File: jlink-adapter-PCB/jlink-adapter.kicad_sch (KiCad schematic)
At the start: 13 parts, among them J1 Conn_02x10_Odd_Even, J2 Conn_02x05_Odd_Even, J3 Conn_02x05_Odd_Even, Q1 BSS123TA

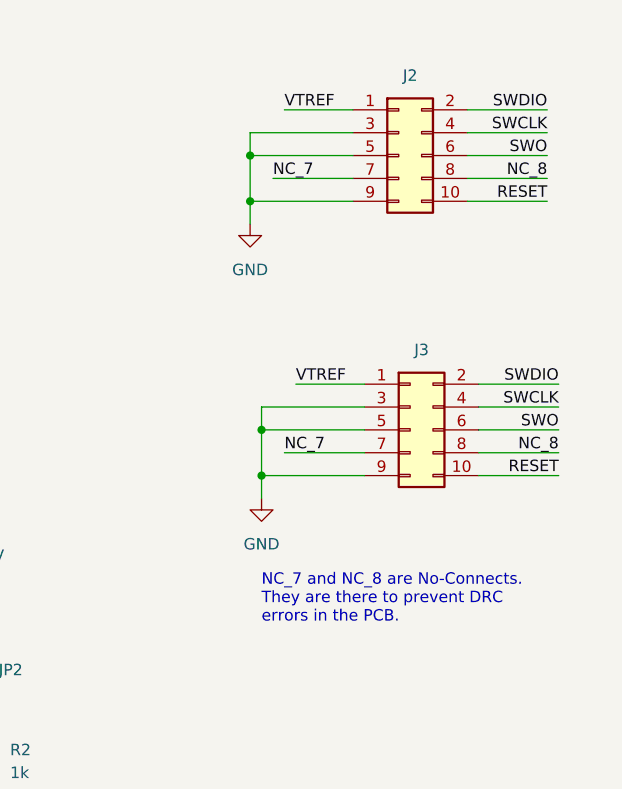
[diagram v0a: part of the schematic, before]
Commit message: Consolidate 10-pin connection on schematic
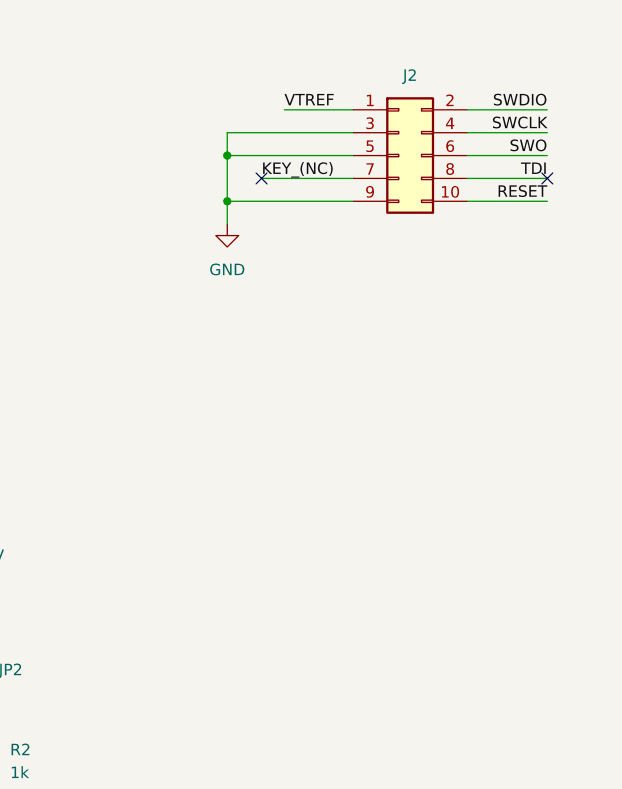
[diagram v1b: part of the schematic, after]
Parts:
- removed J3: Conn_02x05_Odd_Even, Connector_PinHeader_1.27mm:PinHeader_2x05_P1.27mm_Vertical_SMD, symbol Connector_Generic:Conn_02x05_Odd_Even
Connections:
- net NC_7 renamed KEY_(NC)
- net NC_8 renamed TDI
- no-connect marks 9 -> 11
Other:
- note removed: "NC_7 and NC_8 are No-Connects. They are there to prevent DRC errors in the PCB."
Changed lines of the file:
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@@
   (junction (at 93.98 124.46) (diameter 0) (color 0 0 0 0)
   )
-  (junction (at 147.32 67.31) (diameter 0) (color 0 0 0 0)
-  )
-  (junction (at 147.32 72.39) (diameter 0) (color 0 0 0 0)
-  )
-  (junction (at 146.05 36.83) (diameter 0) (color 0 0 0 0)
+  (junction (at 143.51 36.83) (diameter 0) (color 0 0 0 0)
   )
   (junction (at 34.29 45.72) (diameter 0) (color 0 0 0 0)
@@
   (junction (at 71.12 31.75) (diameter 0) (color 0 0 0 0)
   )
-  (junction (at 146.05 41.91) (diameter 0) (color 0 0 0 0)
+  (junction (at 143.51 41.91) (diameter 0) (color 0 0 0 0)
   )
   (junction (at 71.12 39.37) (diameter 0) (color 0 0 0 0)
@@
   (no_connect (at 66.04 49.53))
   (no_connect (at 66.04 46.99))
+  (no_connect (at 147.32 39.37))
   (no_connect (at 53.34 31.75))
   (no_connect (at 66.04 26.67))
+  (no_connect (at 179.07 39.37))
   (no_connect (at 53.34 39.37))
   (no_connect (at 53.34 46.99))
@@
     (stroke (width 0) (type default))
   )
-  (wire (pts (xy 146.05 36.83) (xy 157.48 36.83))
-    (stroke (width 0) (type default))
-  )
-  (wire (pts (xy 146.05 41.91) (xy 157.48 41.91))
+  (wire (pts (xy 143.51 36.83) (xy 157.48 36.83))
+    (stroke (width 0) (type default))
+  )
+  (wire (pts (xy 143.51 41.91) (xy 157.48 41.91))
     (stroke (width 0) (type default))
   )
@@
     (stroke (width 0) (type default))
   )
-  (wire (pts (xy 147.32 72.39) (xy 147.32 74.93))
-    (stroke (width 0) (type default))
-  )
   (wire (pts (xy 170.18 39.37) (xy 179.07 39.37))
     (stroke (width 0) (type default))
@@
     (stroke (width 0) (type default))
   )
-  (wire (pts (xy 171.45 69.85) (xy 180.34 69.85))
-    (stroke (width 0) (type default))
-  )
-  (wire (pts (xy 171.45 72.39) (xy 180.34 72.39))
-    (stroke (width 0) (type default))
-  )
   (wire (pts (xy 106.68 127) (xy 106.68 124.46))
     (stroke (width 0) (type default))
@@
     (stroke (width 0) (type default))
   )
-  (wire (pts (xy 146.05 34.29) (xy 157.48 34.29))
-    (stroke (width 0) (type default))
-  )
-  (wire (pts (xy 151.13 62.23) (xy 158.75 62.23))
-    (stroke (width 0) (type default))
-  )
-  (wire (pts (xy 146.05 41.91) (xy 146.05 44.45))
+  (wire (pts (xy 143.51 34.29) (xy 157.48 34.29))
+    (stroke (width 0) (type default))
+  )
+  (wire (pts (xy 143.51 41.91) (xy 143.51 44.45))
     (stroke (width 0) (type default))
   )
@@
     (stroke (width 0) (type default))
   )
-  (wire (pts (xy 147.32 64.77) (xy 147.32 67.31))
-    (stroke (width 0) (type default))
-  )
-  (wire (pts (xy 148.59 39.37) (xy 157.48 39.37))
-    (stroke (width 0) (type default))
-  )
   (wire (pts (xy 44.45 44.45) (xy 53.34 44.45))
     (stroke (width 0) (type default))
@@
     (stroke (width 0) (type default))
   )
-  (wire (pts (xy 146.05 34.29) (xy 146.05 36.83))
+  (wire (pts (xy 143.51 34.29) (xy 143.51 36.83))
     (stroke (width 0) (type default))
   )
@@
     (stroke (width 0) (type default))
   )
-  (wire (pts (xy 147.32 64.77) (xy 158.75 64.77))
-    (stroke (width 0) (type default))
-  )
   (wire (pts (xy 72.39 124.46) (xy 80.01 124.46))
     (stroke (width 0) (type default))
@@
     (stroke (width 0) (type default))
   )
-  (wire (pts (xy 171.45 67.31) (xy 180.34 67.31))
-    (stroke (width 0) (type default))
-  )
   (wire (pts (xy 71.12 31.75) (xy 71.12 34.29))
     (stroke (width 0) (type default))
@@
     (stroke (width 0) (type default))
   )
-  (wire (pts (xy 146.05 36.83) (xy 146.05 41.91))
+  (wire (pts (xy 143.51 36.83) (xy 143.51 41.91))
+    (stroke (width 0) (type default))
+  )
+  (wire (pts (xy 147.32 39.37) (xy 157.48 39.37))
     (stroke (width 0) (type default))
   )
@@
     (stroke (width 0) (type default))
   )
-  (wire (pts (xy 171.45 64.77) (xy 180.34 64.77))
-    (stroke (width 0) (type default))
-  )
-  (wire (pts (xy 149.86 69.85) (xy 158.75 69.85))
-    (stroke (width 0) (type default))
-  )
-  (wire (pts (xy 147.32 67.31) (xy 158.75 67.31))
-    (stroke (width 0) (type default))
-  )
   (wire (pts (xy 170.18 36.83) (xy 179.07 36.83))
     (stroke (width 0) (type default))
@@
     (stroke (width 0) (type default))
   )
-  (wire (pts (xy 171.45 62.23) (xy 180.34 62.23))
-    (stroke (width 0) (type default))
-  )
   (wire (pts (xy 71.12 39.37) (xy 66.04 39.37))
     (stroke (width 0) (type default))
@@
     (stroke (width 0) (type default))
   )
-  (wire (pts (xy 147.32 67.31) (xy 147.32 72.39))
-    (stroke (width 0) (type default))
-  )
-  (wire (pts (xy 147.32 72.39) (xy 158.75 72.39))
-    (stroke (width 0) (type default))
-  )
   (wire (pts (xy 53.34 49.53) (xy 34.29 49.53))
     (stroke (width 0) (type default))
-  )
-  (text "NC_7 and NC_8 are No-Connects.\nThey are there to prevent DRC\nerrors in the PCB."
-    (at 147.32 88.9 0)
-    (effects (font (size 1.27 1.27)) (justify left bottom))
-  )
-  (label "SWCLK" (at 180.34 64.77 180) (fields_autoplaced)
-    (effects (font (size 1.27 1.27)) (justify right bottom))
-  )
-  (label "NC_7" (at 149.86 69.85 0) (fields_autoplaced)
-    (effects (font (size 1.27 1.27)) (justify left bottom))
-  )
-  (label "NC_8" (at 180.34 69.85 180) (fields_autoplaced)
-    (effects (font (size 1.27 1.27)) (justify right bottom))
   )
   (label "SWDIO" (at 44.45 34.29 0) (fields_autoplaced)
@@
     (effects (font (size 1.27 1.27)) (justify right bottom))
   )
-  (label "NC_8" (at 179.07 39.37 180) (fields_autoplaced)
+  (label "TDI" (at 179.07 39.37 180) (fields_autoplaced)
     (effects (font (size 1.27 1.27)) (justify right bottom))
   )
@@
     (effects (font (size 1.27 1.27)) (justify right bottom))
   )
-  (label "RESET" (at 180.34 72.39 180) (fields_autoplaced)
-    (effects (font (size 1.27 1.27)) (justify right bottom))
-  )
   (label "SWDIO" (at 179.07 31.75 180) (fields_autoplaced)
     (effects (font (size 1.27 1.27)) (justify right bottom))
@@
     (effects (font (size 1.27 1.27)) (justify right bottom))
   )
-  (label "NC_7" (at 148.59 39.37 0) (fields_autoplaced)
+  (label "KEY_(NC)" (at 147.32 39.37 0) (fields_autoplaced)
     (effects (font (size 1.27 1.27)) (justify left bottom))
-  )
-  (label "SWDIO" (at 180.34 62.23 180) (fields_autoplaced)
-    (effects (font (size 1.27 1.27)) (justify right bottom))
   )
   (label "VTREF" (at 44.45 26.67 0) (fields_autoplaced)
@@
   )
   (label "SWO" (at 44.45 41.91 0) (fields_autoplaced)
-    (effects (font (size 1.27 1.27)) (justify left bottom))
-  )
-  (label "SWO" (at 180.34 67.31 180) (fields_autoplaced)
-    (effects (font (size 1.27 1.27)) (justify right bottom))
-  )
-  (label "VTREF" (at 151.13 62.23 0) (fields_autoplaced)
     (effects (font (size 1.27 1.27)) (justify left bottom))
   )
@@
     )
   )
-  (symbol (lib_id "power:GND") (at 146.05 44.45 0) (unit 1)
-    (in_bom yes) (on_board yes) (dnp no) (fields_autoplaced)
-    (property "Reference" "#PWR03" (at 146.05 50.8 0)
-      (effects (font (size 1.27 1.27)) hide)
-    )
-    (property "Value" "GND" (at 146.05 49.53 0)
-      (effects (font (size 1.27 1.27)))
-    )
-    (property "Footprint" "" (at 146.05 44.45 0)
-      (effects (font (size 1.27 1.27)) hide)
-    )
-    (property "Datasheet" "" (at 146.05 44.45 0)
+  (symbol (lib_id "power:GND") (at 143.51 44.45 0) (unit 1)
+    (in_bom yes) (on_board yes) (dnp no) (fields_autoplaced)
+    (property "Reference" "#PWR03" (at 143.51 50.8 0)
+      (effects (font (size 1.27 1.27)) hide)
+    )
+    (property "Value" "GND" (at 143.51 49.53 0)
+      (effects (font (size 1.27 1.27)))
+    )
+    (property "Footprint" "" (at 143.51 44.45 0)
+      (effects (font (size 1.27 1.27)) hide)
+    )
+    (property "Datasheet" "" (at 143.51 44.45 0)
       (effects (font (size 1.27 1.27)) hide)
     )
@@
     )
   )
-  (symbol (lib_id "power:GND") (at 147.32 74.93 0) (unit 1)
-    (in_bom yes) (on_board yes) (dnp no) (fields_autoplaced)
-    (property "Reference" "#PWR09" (at 147.32 81.28 0)
-      (effects (font (size 1.27 1.27)) hide)
-    )
-    (property "Value" "GND" (at 147.32 80.01 0)
-      (effects (font (size 1.27 1.27)))
-    )
-    (property "Footprint" "" (at 147.32 74.93 0)
-      (effects (font (size 1.27 1.27)) hide)
-    )
-    (property "Datasheet" "" (at 147.32 74.93 0)
-      (effects (font (size 1.27 1.27)) hide)
-    )
-    (pin "1")
-    (instances
-      (project "jlink-adapter"
-        (path "/c4b4938f-57db-4256-8168-815a3371e956"
-          (reference "#PWR09") (unit 1)
-        )
-      )
-    )
-  )
   (symbol (lib_id "Device:R_Small") (at 48.26 106.68 0) (unit 1)
     (in_bom yes) (on_board yes) (dnp no) (fields_autoplaced)
@@
         )
       )
-    )
-  )
-  (symbol (lib_id "Connector_Generic:Conn_02x05_Odd_Even") (at 163.83 67.31 0) (unit 1)
-    (in_bom yes) (on_board yes) (dnp no)
-    (property "Reference" "J3" (at 165.1 58.42 0)
-      (effects (font (size 1.27 1.27)))
-    )
-    (property "Value" "Conn_02x05_Odd_Even" (at 165.1 59.055 0)
-      (effects (font (size 1.27 1.27)) hide)
-    )
-    (property "Footprint" "Connector_PinHeader_1.27mm:PinHeader_2x05_P1.27mm_Vertical_SMD" (at 163.83 67.31 0)
-      (effects (font (size 1.27 1.27)) hide)
-    )
-    (property "Datasheet" "~" (at 163.83 67.31 0)
-      (effects (font (size 1.27 1.27)) hide)
-    )
-    (pin "1")
-    (pin "10")
-    (pin "2")
-    (pin "3")
-    (pin "4")
-    (pin "5")
-    (pin "6")
-    (pin "7")
-    (pin "8")
-    (pin "9")
-    (instances
-      (project "jlink-adapter"
-        (path "/c4b4938f-57db-4256-8168-815a3371e956"
-          (reference "J3") (unit 1)
-        )
-      )

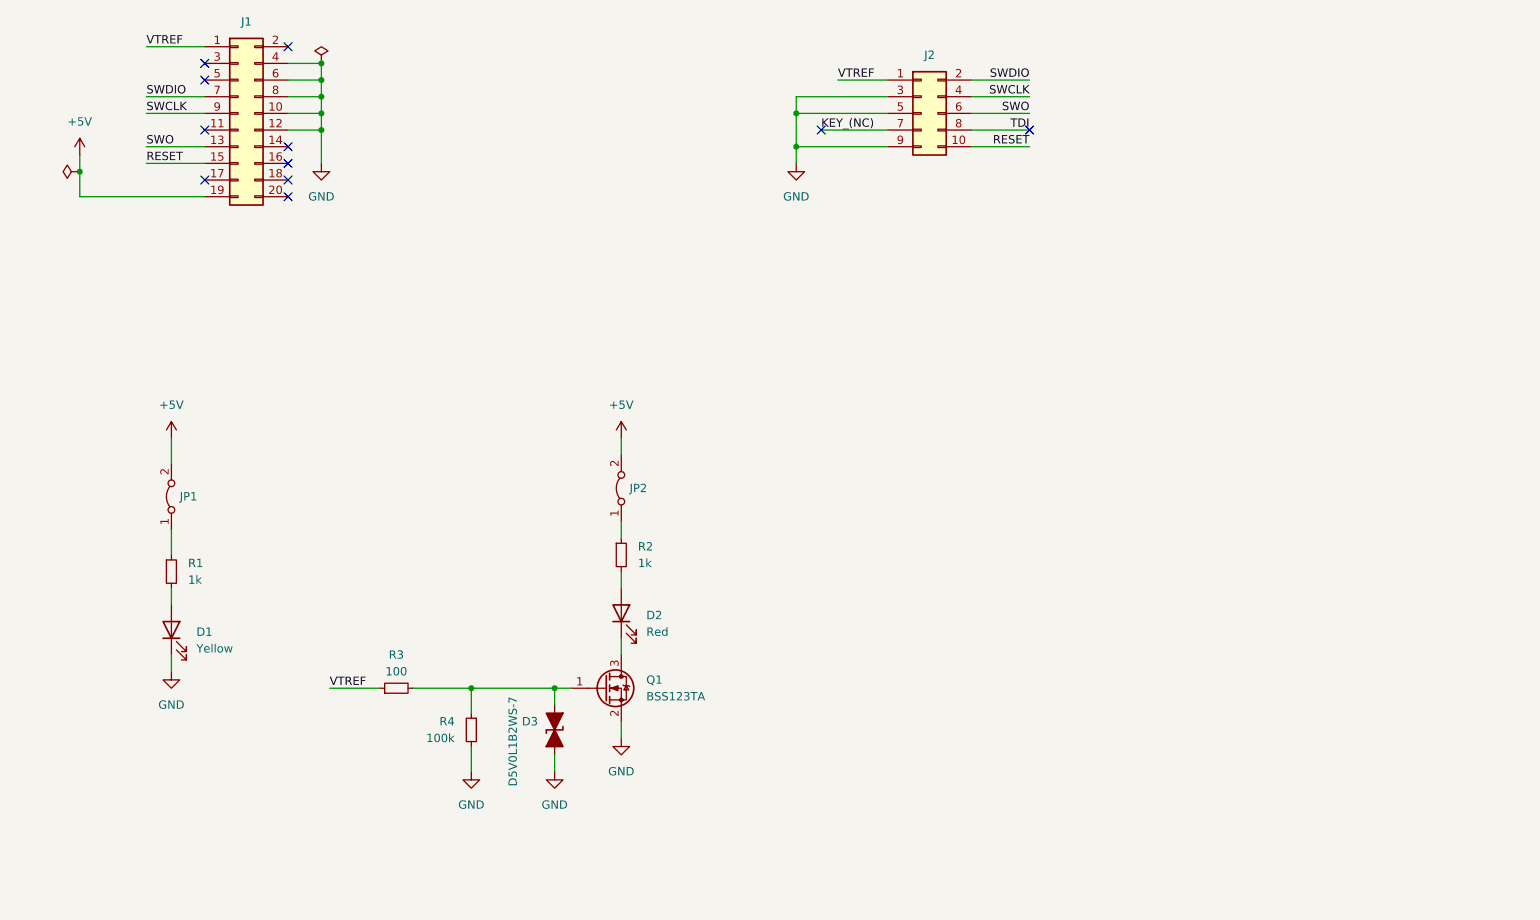
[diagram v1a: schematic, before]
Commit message: Fix the footprint for JLink and add comments
The footprint used for the 20-pin connector ended up being backwards wrt
Jlink connection.  Using the PinSocket family fixes this without having
to draw a custom connector.

Added comments and meta-data to the schematic
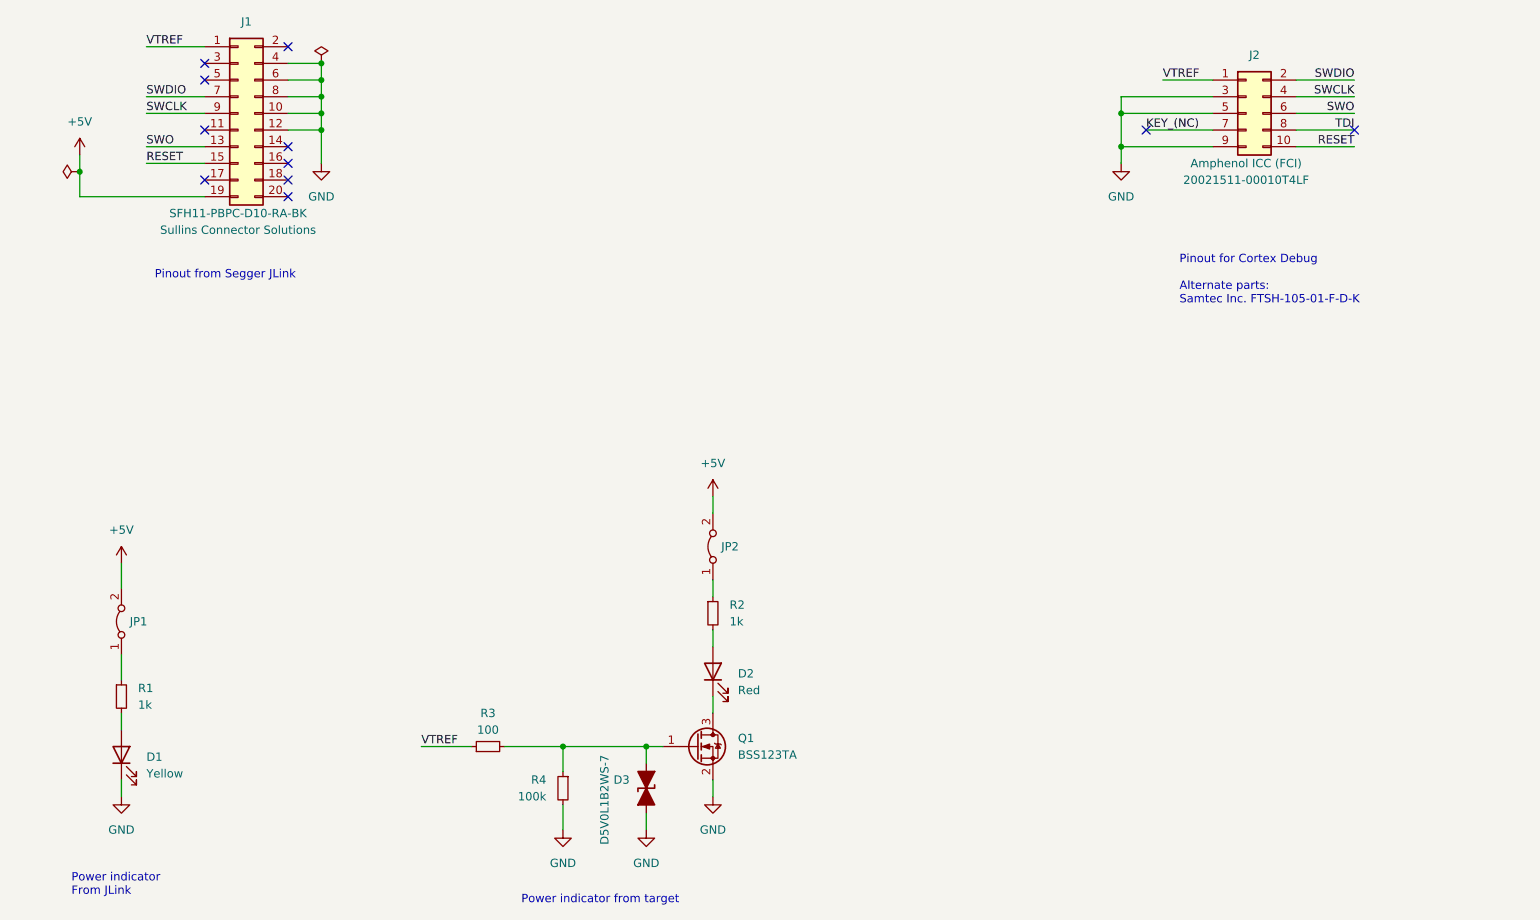
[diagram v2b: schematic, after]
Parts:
- J1: footprint Connector_PinHeader_2.54mm:PinHeader_2x10_P2.54mm_Horizontal -> Connector_PinSocket_2.54mm:PinSocket_2x10_P2.54mm_Horizontal
- J2: Mfg (none) -> Amphenol ICC (FCI); Part Num (none) -> 20021511-00010T4LF
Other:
- note added: "Pinout for Cortex Debug Alternate parts: Samtec Inc. FTSH-105-01-F-D-K"
- note added: "Pinout from Segger JLink"
- note added: "Power indicator From JLink"
- note added: "Power indicator from target"
- moved on the sheet: D1, D2, D3, J2, JP1, JP2, Q1, R1, R2, R3, R4

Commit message: Finalize V2 of Jlink adapter
Cleaned up more DRC errors
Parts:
- J1: footprint Connector_PinSocket_2.54mm:PinSocket_2x10_P2.54mm_Horizontal -> JLink-adapter:PinSocket_2x10_P2.54mm_Horizontal_clipped_silkscreen
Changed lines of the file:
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@@
       (effects (font (size 1.27 1.27)) hide)
     )
-    (property "Footprint" "Connector_PinSocket_2.54mm:PinSocket_2x10_P2.54mm_Horizontal" (at 58.42 36.83 0)
+    (property "Footprint" "JLink-adapter:PinSocket_2x10_P2.54mm_Horizontal_clipped_silkscreen" (at 58.42 36.83 0)
       (effects (font (size 1.27 1.27)) hide)
     )

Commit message: V3 of the Jlink board
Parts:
- added J3: Tag-Connect IDC, Connector_IDC:IDC-Header_2x03_P2.54mm_Vertical, symbol Connector:Conn_ARM_SWD_TagConnect_TC2030
- JP1, JP2: now left out of the parts list
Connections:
- net GND: now also J3.5 (GND)
- net RESET: now also J3.3 (~{RESET})
- net SWCLK: now also J3.4 (SWCLK)
- net SWDIO: now also J3.2 (SWDIO)
- net SWO: now also J3.6 (SWO)
- net VTREF: now also J3.1 (VCC)

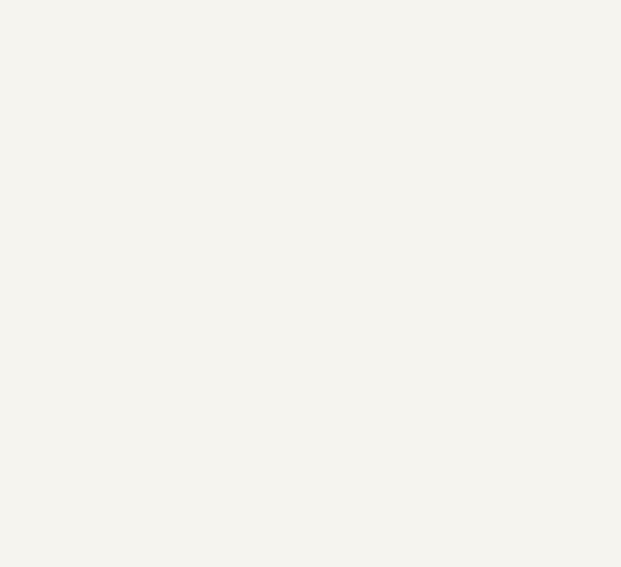
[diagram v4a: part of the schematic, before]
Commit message: Add feedback from V3 build, and update README
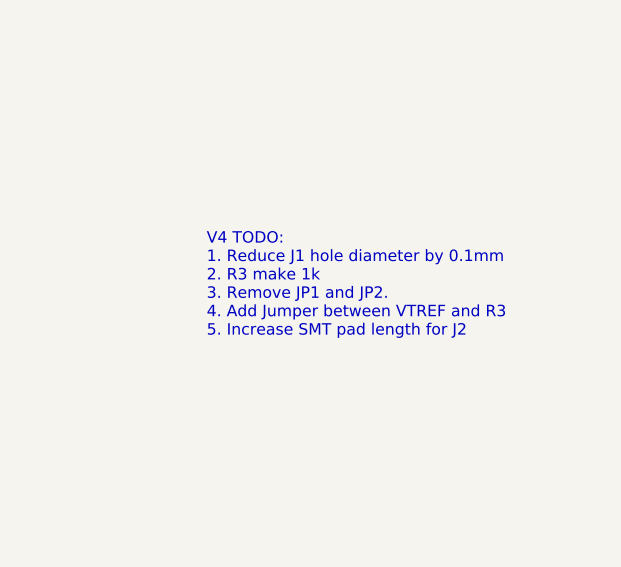
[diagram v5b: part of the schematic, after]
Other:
- note added: "V4 TODO: 1. Reduce J1 hole diameter by 0.1mm 2. R3 make 1k 3. Remove JP1 and JP2. 4. Add Jumper between VTREF and R3 5. Increase SMT pad length for J2"
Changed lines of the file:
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@@
+		)
+	)
+	(text "V4 TODO:\n1. Reduce J1 hole diameter by 0.1mm\n2. R3 make 1k\n3. Remove JP1 and JP2.\n4. Add Jumper between VTREF and R3\n5. Increase SMT pad length for J2"
+		(exclude_from_sim no)
+		(at 210.82 102.87 0)
+		(effects
+			(font
+				(size 1.27 1.27)
+			)
+			(justify left)
 		)
 	)
